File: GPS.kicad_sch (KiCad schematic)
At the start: 17 parts, among them Q5 Q_NPN_BCE, Q6 Q_NMOS_DGS, Q7 Q_PMOS_DGS, U10 L96-M33

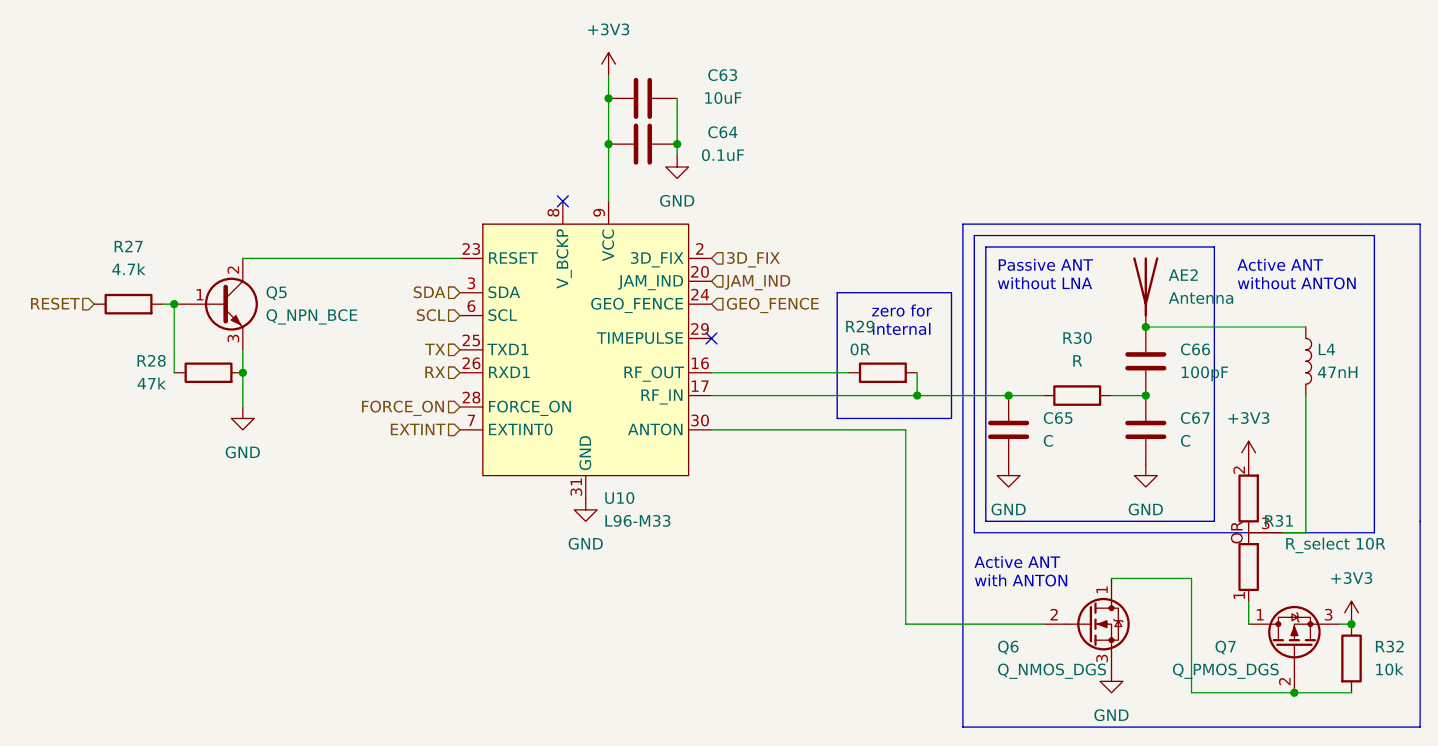
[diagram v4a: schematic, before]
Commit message: PI LC lowpass filter, added CP2012 reset, added connectors
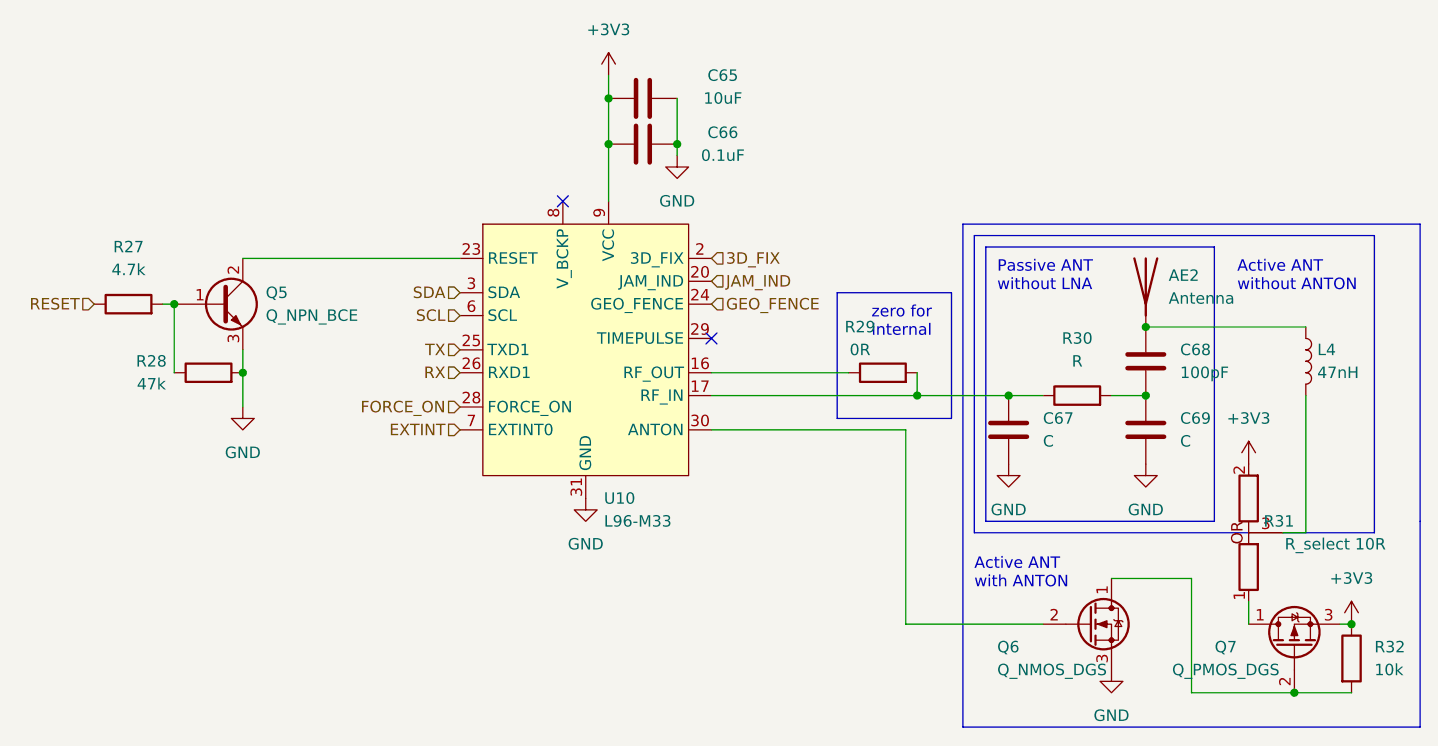
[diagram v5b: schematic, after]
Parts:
- renumbered C63 to C65, C64 to C66, C65 to C67, C66 to C68, C67 to C69
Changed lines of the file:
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@@
   (symbol (lib_id "power:GND") (at 201.93 100.33 0) (unit 1)
     (in_bom yes) (on_board yes) (fields_autoplaced)
-    (property "Reference" "#PWR083" (id 0) (at 201.93 106.68 0)
+    (property "Reference" "#PWR082" (id 0) (at 201.93 106.68 0)
       (effects (font (size 1.27 1.27)) hide)
     )
@@
   (symbol (lib_id "Device:C") (at 201.93 88.9 180) (unit 1)
     (in_bom yes) (on_board yes)
-    (property "Reference" "C66" (id 0) (at 205.74 87.6299 0)
+    (property "Reference" "C68" (id 0) (at 205.74 87.6299 0)
       (effects (font (size 1.27 1.27)) (justify right))
     )
@@
   (symbol (lib_id "power:+3V3") (at 213.36 100.33 0) (unit 1)
     (in_bom yes) (on_board yes) (fields_autoplaced)
-    (property "Reference" "#PWR084" (id 0) (at 213.36 104.14 0)
+    (property "Reference" "#PWR083" (id 0) (at 213.36 104.14 0)
       (effects (font (size 1.27 1.27)) hide)
     )
@@
   (symbol (lib_id "Device:C") (at 146.05 64.77 270) (mirror x) (unit 1)
     (in_bom yes) (on_board yes)
-    (property "Reference" "C64" (id 0) (at 154.94 63.5 90))
+    (property "Reference" "C66" (id 0) (at 154.94 63.5 90))
     (property "Value" "0.1uF" (id 1) (at 154.94 66.04 90))
     (property "Footprint" "" (id 2) (at 142.24 63.8048 0)
@@
   (symbol (lib_id "Device:C") (at 201.93 96.52 0) (unit 1)
     (in_bom yes) (on_board yes) (fields_autoplaced)
-    (property "Reference" "C67" (id 0) (at 205.74 95.2499 0)
+    (property "Reference" "C69" (id 0) (at 205.74 95.2499 0)
       (effects (font (size 1.27 1.27)) (justify left))
     )
@@
   (symbol (lib_id "power:GND") (at 186.69 100.33 0) (unit 1)
     (in_bom yes) (on_board yes) (fields_autoplaced)
-    (property "Reference" "#PWR081" (id 0) (at 186.69 106.68 0)
+    (property "Reference" "#PWR080" (id 0) (at 186.69 106.68 0)
       (effects (font (size 1.27 1.27)) hide)
     )
@@
   (symbol (lib_id "Device:C") (at 186.69 96.52 0) (unit 1)
     (in_bom yes) (on_board yes) (fields_autoplaced)
-    (property "Reference" "C65" (id 0) (at 190.5 95.2499 0)
+    (property "Reference" "C67" (id 0) (at 190.5 95.2499 0)
       (effects (font (size 1.27 1.27)) (justify left))
     )
@@
   (symbol (lib_id "power:GND") (at 139.7 104.14 0) (unit 1)
     (in_bom yes) (on_board yes) (fields_autoplaced)
-    (property "Reference" "#PWR078" (id 0) (at 139.7 110.49 0)
+    (property "Reference" "#PWR077" (id 0) (at 139.7 110.49 0)
       (effects (font (size 1.27 1.27)) hide)
     )
@@
   (symbol (lib_id "power:+3V3") (at 142.24 57.15 0) (mirror y) (unit 1)
     (in_bom yes) (on_board yes) (fields_autoplaced)
-    (property "Reference" "#PWR079" (id 0) (at 142.24 60.96 0)
+    (property "Reference" "#PWR078" (id 0) (at 142.24 60.96 0)
       (effects (font (size 1.27 1.27)) hide)
     )
@@
   (symbol (lib_id "power:GND") (at 101.6 93.98 0) (unit 1)
     (in_bom yes) (on_board yes) (fields_autoplaced)
-    (property "Reference" "#PWR077" (id 0) (at 101.6 100.33 0)
+    (property "Reference" "#PWR076" (id 0) (at 101.6 100.33 0)
       (effects (font (size 1.27 1.27)) hide)
     )
@@
   (symbol (lib_id "Device:C") (at 146.05 59.69 270) (mirror x) (unit 1)
     (in_bom yes) (on_board yes)
-    (property "Reference" "C63" (id 0) (at 154.94 57.15 90))
+    (property "Reference" "C65" (id 0) (at 154.94 57.15 90))
     (property "Value" "10uF" (id 1) (at 154.94 59.69 90))
     (property "Footprint" "" (id 2) (at 142.24 58.7248 0)
@@
   (symbol (lib_id "power:GND") (at 149.86 66.04 0) (mirror y) (unit 1)
     (in_bom yes) (on_board yes) (fields_autoplaced)
-    (property "Reference" "#PWR080" (id 0) (at 149.86 72.39 0)
+    (property "Reference" "#PWR079" (id 0) (at 149.86 72.39 0)
       (effects (font (size 1.27 1.27)) hide)
     )
@@
   (symbol (lib_id "power:+3V3") (at 224.79 118.11 0) (unit 1)
     (in_bom yes) (on_board yes) (fields_autoplaced)
-    (property "Reference" "#PWR085" (id 0) (at 224.79 121.92 0)
+    (property "Reference" "#PWR084" (id 0) (at 224.79 121.92 0)
       (effects (font (size 1.27 1.27)) hide)
     )
@@
   (symbol (lib_id "power:GND") (at 198.12 123.19 0) (unit 1)
     (in_bom yes) (on_board yes) (fields_autoplaced)
-    (property "Reference" "#PWR082" (id 0) (at 198.12 129.54 0)
-      (effects (font (size 1.27 1.27)) hide)
-    )
+    (property "Reference" "#PWR081" (id 0) (at 198.12 129.54 0)
+      (effects (font (size 1.27 1.27)) hide)
+    )

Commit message: datasheet checkout, added couple of capacitors for usb-c, groupd some scheatics
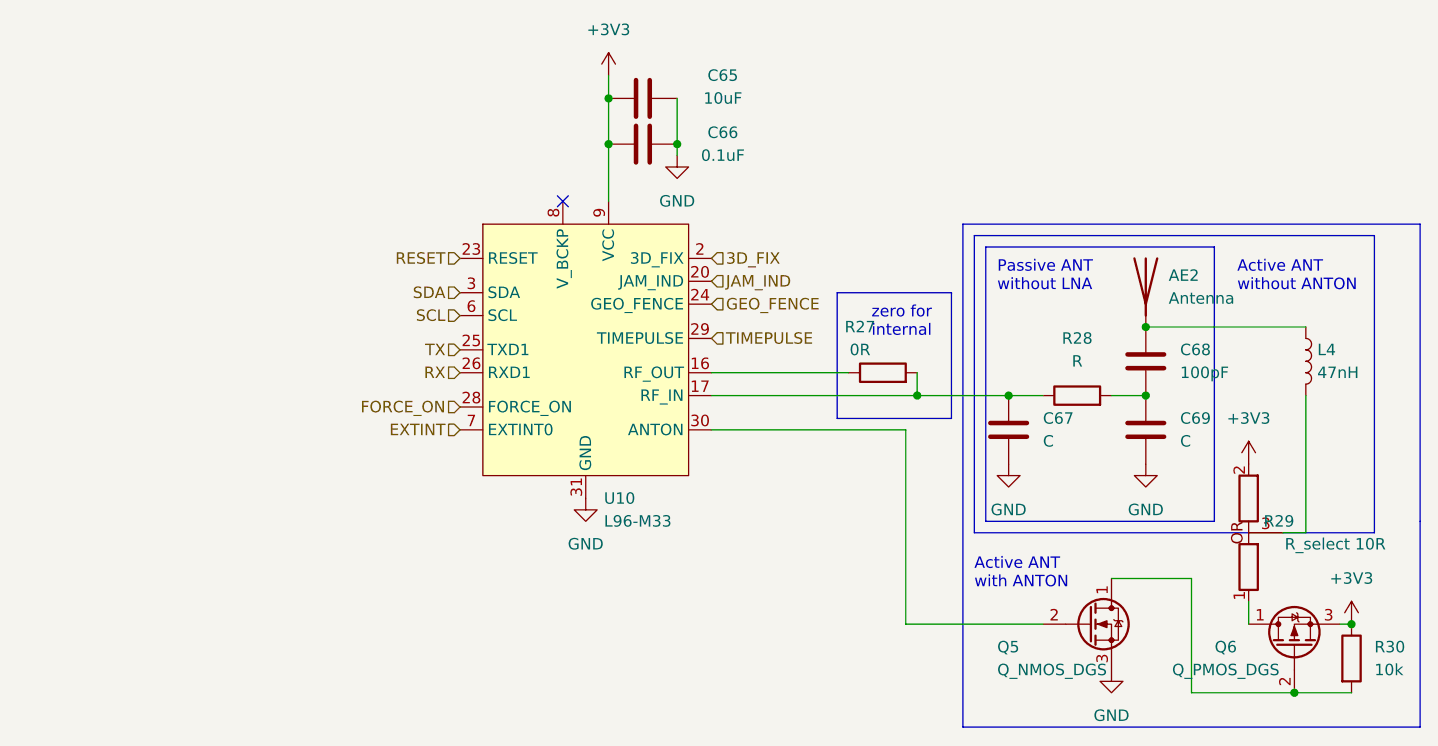
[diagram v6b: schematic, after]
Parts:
- removed Q5: Q_NPN_BCE, symbol Device:Q_NPN_BCE
- removed R27: 4.7k, symbol Device:R
- removed R28: 47k, symbol Device:R
- renumbered Q6 to Q5, Q7 to Q6, R29 to R27, R30 to R28, R31 to R29, R32 to R30
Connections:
- net RESET: now also U10.23 (RESET)
- net TIMEPULSE: now reaches U10.29 (TIMEPULSE)
- no-connect marks 2 -> 1
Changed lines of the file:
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@@
   (junction (at 142.24 64.77) (diameter 0) (color 0 0 0 0)
   )
-  (junction (at 101.6 90.17) (diameter 0) (color 0 0 0 0)
-  )
   (junction (at 186.69 92.71) (diameter 0) (color 0 0 0 0)
   )
   (junction (at 142.24 59.69) (diameter 0) (color 0 0 0 0)
   )
-  (junction (at 93.98 82.55) (diameter 0) (color 0 0 0 0)
-  )
   (junction (at 149.86 64.77) (diameter 0) (color 0 0 0 0)
   )
@@
   (junction (at 201.93 85.09) (diameter 0) (color 0 0 0 0)
   )
-  (no_connect (at 153.67 86.36))
   (no_connect (at 137.16 71.12))
   (wire (pts (xy 149.86 64.77) (xy 149.86 66.04))
@@
     (stroke (width 0) (type default) (color 0 0 0 0))
   )
-  (wire (pts (xy 101.6 87.63) (xy 101.6 90.17))
-    (stroke (width 0) (type default) (color 0 0 0 0))
-  )
   (wire (pts (xy 224.79 118.11) (xy 223.52 118.11))
     (stroke (width 0) (type default) (color 0 0 0 0))
@@
     (stroke (width 0) (type default) (color 0 0 0 0))
   )
-  (wire (pts (xy 101.6 90.17) (xy 101.6 93.98))
-    (stroke (width 0) (type default) (color 0 0 0 0))
-  )
   (wire (pts (xy 213.36 115.57) (xy 213.36 118.11))
     (stroke (width 0) (type default) (color 0 0 0 0))
@@
     (stroke (width 0) (type default) (color 0 0 0 0))
   )
-  (wire (pts (xy 92.71 82.55) (xy 93.98 82.55))
-    (stroke (width 0) (type default) (color 0 0 0 0))
-  )
   (wire (pts (xy 142.24 64.77) (xy 142.24 71.12))
     (stroke (width 0) (type default) (color 0 0 0 0))
@@
     (stroke (width 0) (type default) (color 0 0 0 0))
   )
-  (wire (pts (xy 101.6 77.47) (xy 125.73 77.47))
-    (stroke (width 0) (type default) (color 0 0 0 0))
-  )
   (wire (pts (xy 219.71 107.95) (xy 217.17 107.95))
     (stroke (width 0) (type default) (color 0 0 0 0))
@@
   )
   (polyline (pts (xy 232.41 73.66) (xy 232.41 106.68))
-    (stroke (width 0) (type default) (color 0 0 0 0))
-  )
-  (wire (pts (xy 93.98 82.55) (xy 93.98 90.17))
     (stroke (width 0) (type default) (color 0 0 0 0))
   )
@@
     (effects (font (size 1.27 1.27)) (justify left bottom))
   )
+  (hierarchical_label "TIMEPULSE" (shape input) (at 153.67 86.36 0)
+    (effects (font (size 1.27 1.27)) (justify left))
+  )
   (hierarchical_label "FORCE_ON" (shape input) (at 125.73 93.98 180)
     (effects (font (size 1.27 1.27)) (justify right))
@@
     (effects (font (size 1.27 1.27)) (justify left))
   )
-  (hierarchical_label "RESET" (shape input) (at 85.09 82.55 180)
+  (hierarchical_label "RESET" (shape input) (at 125.73 77.47 180)
     (effects (font (size 1.27 1.27)) (justify right))
   )
@@
   (symbol (lib_id "Device:R") (at 172.72 90.17 90) (unit 1)
     (in_bom yes) (on_board yes)
-    (property "Reference" "R29" (id 0) (at 170.18 85.09 90))
+    (property "Reference" "R27" (id 0) (at 170.18 85.09 90))
     (property "Value" "0R" (id 1) (at 170.18 87.63 90))
     (property "Footprint" "" (id 2) (at 172.72 91.948 90)
@@
   (symbol (lib_id "power:GND") (at 201.93 100.33 0) (unit 1)
     (in_bom yes) (on_board yes) (fields_autoplaced)
-    (property "Reference" "#PWR082" (id 0) (at 201.93 106.68 0)
+    (property "Reference" "#PWR081" (id 0) (at 201.93 106.68 0)
       (effects (font (size 1.27 1.27)) hide)
     )
@@
   (symbol (lib_id "power:+3V3") (at 213.36 100.33 0) (unit 1)
     (in_bom yes) (on_board yes) (fields_autoplaced)
-    (property "Reference" "#PWR083" (id 0) (at 213.36 104.14 0)
+    (property "Reference" "#PWR082" (id 0) (at 213.36 104.14 0)
       (effects (font (size 1.27 1.27)) hide)
     )
@@
   (symbol (lib_id "Device:Q_NMOS_DGS") (at 195.58 118.11 0) (unit 1)
     (in_bom yes) (on_board yes)
-    (property "Reference" "Q6" (id 0) (at 185.42 120.65 0)
+    (property "Reference" "Q5" (id 0) (at 185.42 120.65 0)
       (effects (font (size 1.27 1.27)) (justify left))
     )
@@
   (symbol (lib_id "power:GND") (at 186.69 100.33 0) (unit 1)
     (in_bom yes) (on_board yes) (fields_autoplaced)
-    (property "Reference" "#PWR080" (id 0) (at 186.69 106.68 0)
+    (property "Reference" "#PWR079" (id 0) (at 186.69 106.68 0)
       (effects (font (size 1.27 1.27)) hide)
     )
@@
   (symbol (lib_id "airsoft_controller:R_select") (at 213.36 107.95 180) (unit 1)
     (in_bom yes) (on_board yes)
-    (property "Reference" "R31" (id 0) (at 218.44 106.68 0)
+    (property "Reference" "R29" (id 0) (at 218.44 106.68 0)
       (effects (font (size 1.27 1.27)) (justify left))
     )
@@
     (pin "2")
   )
-  (symbol (lib_id "Device:Q_NPN_BCE") (at 99.06 82.55 0) (unit 1)
-    (in_bom yes) (on_board yes) (fields_autoplaced)
-    (property "Reference" "Q5" (id 0) (at 104.14 81.2799 0)
-      (effects (font (size 1.27 1.27)) (justify left))
-    )
-    (property "Value" "Q_NPN_BCE" (id 1) (at 104.14 83.8199 0)
-      (effects (font (size 1.27 1.27)) (justify left))
-    )
-    (property "Footprint" "" (id 2) (at 104.14 80.01 0)
-      (effects (font (size 1.27 1.27)) hide)
-    )
-    (property "Datasheet" "~" (id 3) (at 99.06 82.55 0)
-      (effects (font (size 1.27 1.27)) hide)
-    )
-    (pin "1")
-    (pin "2")
-    (pin "3")
-  )
   (symbol (lib_id "power:GND") (at 139.7 104.14 0) (unit 1)
     (in_bom yes) (on_board yes) (fields_autoplaced)
-    (property "Reference" "#PWR077" (id 0) (at 139.7 110.49 0)
+    (property "Reference" "#PWR076" (id 0) (at 139.7 110.49 0)
       (effects (font (size 1.27 1.27)) hide)
     )
@@
   (symbol (lib_id "Device:Q_PMOS_DGS") (at 218.44 120.65 90) (unit 1)
     (in_bom yes) (on_board yes)
-    (property "Reference" "Q7" (id 0) (at 210.82 120.65 90))
+    (property "Reference" "Q6" (id 0) (at 210.82 120.65 90))
     (property "Value" "Q_PMOS_DGS" (id 1) (at 210.82 123.19 90))
     (property "Footprint" "" (id 2) (at 215.9 115.57 0)
@@
     (pin "3")
   )
-  (symbol (lib_id "Device:R") (at 97.79 90.17 90) (unit 1)
-    (in_bom yes) (on_board yes)
-    (property "Reference" "R28" (id 0) (at 91.44 88.9 90))
-    (property "Value" "47k" (id 1) (at 91.44 91.44 90))
-    (property "Footprint" "" (id 2) (at 97.79 91.948 90)
-      (effects (font (size 1.27 1.27)) hide)
-    )
-    (property "Datasheet" "~" (id 3) (at 97.79 90.17 0)
-      (effects (font (size 1.27 1.27)) hide)
-    )
-    (pin "1")
-    (pin "2")
-  )
   (symbol (lib_id "power:+3V3") (at 142.24 57.15 0) (mirror y) (unit 1)
     (in_bom yes) (on_board yes) (fields_autoplaced)
-    (property "Reference" "#PWR078" (id 0) (at 142.24 60.96 0)
+    (property "Reference" "#PWR077" (id 0) (at 142.24 60.96 0)
       (effects (font (size 1.27 1.27)) hide)
     )
@@
     )
     (property "Datasheet" "" (id 3) (at 142.24 57.15 0)
-      (effects (font (size 1.27 1.27)) hide)
-    )
-    (pin "1")
-  )
-  (symbol (lib_id "power:GND") (at 101.6 93.98 0) (unit 1)
-    (in_bom yes) (on_board yes) (fields_autoplaced)
-    (property "Reference" "#PWR076" (id 0) (at 101.6 100.33 0)
-      (effects (font (size 1.27 1.27)) hide)
-    )
-    (property "Value" "GND" (id 1) (at 101.6 99.06 0))
-    (property "Footprint" "" (id 2) (at 101.6 93.98 0)
-      (effects (font (size 1.27 1.27)) hide)
-    )
-    (property "Datasheet" "" (id 3) (at 101.6 93.98 0)
       (effects (font (size 1.27 1.27)) hide)
     )
@@
   (symbol (lib_id "power:GND") (at 149.86 66.04 0) (mirror y) (unit 1)
     (in_bom yes) (on_board yes) (fields_autoplaced)
-    (property "Reference" "#PWR079" (id 0) (at 149.86 72.39 0)
+    (property "Reference" "#PWR078" (id 0) (at 149.86 72.39 0)
       (effects (font (size 1.27 1.27)) hide)
     )
@@
   (symbol (lib_id "power:+3V3") (at 224.79 118.11 0) (unit 1)
     (in_bom yes) (on_board yes) (fields_autoplaced)
-    (property "Reference" "#PWR084" (id 0) (at 224.79 121.92 0)
+    (property "Reference" "#PWR083" (id 0) (at 224.79 121.92 0)
       (effects (font (size 1.27 1.27)) hide)
     )
@@
   (symbol (lib_id "Device:R") (at 224.79 121.92 0) (unit 1)
     (in_bom yes) (on_board yes) (fields_autoplaced)
-    (property "Reference" "R32" (id 0) (at 227.33 120.6499 0)
+    (property "Reference" "R30" (id 0) (at 227.33 120.6499 0)
       (effects (font (size 1.27 1.27)) (justify left))
     )
@@
     (pin "2")
   )
-  (symbol (lib_id "Device:R") (at 88.9 82.55 90) (unit 1)
-    (in_bom yes) (on_board yes) (fields_autoplaced)
-    (property "Reference" "R27" (id 0) (at 88.9 76.2 90))
-    (property "Value" "4.7k" (id 1) (at 88.9 78.74 90))
-    (property "Footprint" "" (id 2) (at 88.9 84.328 90)
-      (effects (font (size 1.27 1.27)) hide)
-    )
-    (property "Datasheet" "~" (id 3) (at 88.9 82.55 0)
-      (effects (font (size 1.27 1.27)) hide)
-    )
-    (pin "1")
-    (pin "2")
-  )
   (symbol (lib_id "Device:R") (at 194.31 92.71 90) (unit 1)
     (in_bom yes) (on_board yes) (fields_autoplaced)
-    (property "Reference" "R30" (id 0) (at 194.31 86.36 90))
+    (property "Reference" "R28" (id 0) (at 194.31 86.36 90))
     (property "Value" "R" (id 1) (at 194.31 88.9 90))
     (property "Footprint" "" (id 2) (at 194.31 94.488 90)
@@
   (symbol (lib_id "power:GND") (at 198.12 123.19 0) (unit 1)
     (in_bom yes) (on_board yes) (fields_autoplaced)
-    (property "Reference" "#PWR081" (id 0) (at 198.12 129.54 0)
-      (effects (font (size 1.27 1.27)) hide)
-    )
+    (property "Reference" "#PWR080" (id 0) (at 198.12 129.54 0)
+      (effects (font (size 1.27 1.27)) hide)
+    )
